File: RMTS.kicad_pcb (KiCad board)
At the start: 2 copper layers, 80 x 50.2 mm, 54 parts, among them J1 USB_B, J10 CONN_02, J2 Programmer, J3 Screw_Terminal_01x03, J4 Screw_Terminal_01x04, J5 Screw_Terminal_01x02, J6 Screw_Terminal_01x02, J7 Micro_SD_Card_Det_Hirose_DM3AT, J8 CONN_03, J9 CONN_02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

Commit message: Fixed mistakes
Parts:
- C11, C12: value C -> 0.1uF
- DRDY: value TestPoint -> DRDY
- R10, R9: value R_US -> 1k
- SCL: value TestPoint -> SCL
- SDA: value TestPoint -> SDA
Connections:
- U3 pad 8: /VBUS -> GND
- U3 pad 9: GND -> /VBUS
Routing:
- net /VBUS: track 128.1 -> 126.5 mm, vias 2 -> 1
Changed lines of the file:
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@@
     (thickness 1.6)
     (drawings 22)
-    (tracks 467)
+    (tracks 468)
     (zones 0)
     (modules 54)
@@
       (effects (font (size 1 1) (thickness 0.15)))
     )
-    (fp_text value TestPoint (at 0 1.55) (layer F.Fab)
+    (fp_text value SCL (at 0 1.55) (layer F.Fab)
       (effects (font (size 1 1) (thickness 0.15)))
     )
@@
       (effects (font (size 1 1) (thickness 0.15)))
     )
-    (fp_text value TestPoint (at 0 1.55) (layer F.Fab)
+    (fp_text value SDA (at 0 1.55) (layer F.Fab)
       (effects (font (size 1 1) (thickness 0.15)))
     )
@@
       (effects (font (size 1 1) (thickness 0.15)))
     )
-    (fp_text value TestPoint (at 0 1.55) (layer F.Fab)
+    (fp_text value DRDY (at 0 1.55) (layer F.Fab)
       (effects (font (size 1 1) (thickness 0.15)))
     )
@@
       (effects (font (size 1 1) (thickness 0.15)))
     )
-    (fp_text value C (at 0 1.65) (layer F.Fab)
+    (fp_text value 0.1uF (at 0 1.65) (layer F.Fab)
       (effects (font (size 1 1) (thickness 0.15)))
     )
@@
       (effects (font (size 1 1) (thickness 0.15)))
     )
-    (fp_text value C (at 0 1.65) (layer F.Fab)
+    (fp_text value 0.1uF (at 0 1.65) (layer F.Fab)
       (effects (font (size 1 1) (thickness 0.15)))
     )
@@
       (effects (font (size 1 1) (thickness 0.15)))
     )
-    (fp_text value R_US (at 0 1.65) (layer F.Fab)
+    (fp_text value 1k (at 0 1.65) (layer F.Fab)
       (effects (font (size 1 1) (thickness 0.15)))
     )
@@
       (effects (font (size 1 1) (thickness 0.15)))
     )
-    (fp_text value R_US (at 0 1.65) (layer F.Fab)
+    (fp_text value 1k (at 0 1.65) (layer F.Fab)
       (effects (font (size 1 1) (thickness 0.15)))
     )
@@
       (net 18 "Net-(J3-Pad3)"))
     (pad 8 smd rect (at -2.95 2.275 90) (size 1.5 0.45) (layers F.Cu F.Paste F.Mask)
+      (net 1 GND))
+    (pad 9 smd rect (at 2.95 2.275 90) (size 1.5 0.45) (layers F.Cu F.Paste F.Mask)
       (net 2 /VBUS))
-    (pad 9 smd rect (at 2.95 2.275 90) (size 1.5 0.45) (layers F.Cu F.Paste F.Mask)
-      (net 1 GND))
     (pad 10 smd rect (at 2.95 1.625 90) (size 1.5 0.45) (layers F.Cu F.Paste F.Mask)
       (net 1 GND))
@@
   (segment (start 201.54 104.53) (end 201.295 104.775) (width 0.2) (layer F.Cu) (net 1))
   (segment (start 201.54 102.87) (end 201.54 104.53) (width 0.2) (layer F.Cu) (net 1))
-  (via (at 202.184 93.726) (size 0.6) (drill 0.4) (layers F.Cu B.Cu) (net 1))
   (via (at 181.61 93.98) (size 0.6) (drill 0.4) (layers F.Cu B.Cu) (net 1))
   (segment (start 181.61 93.98) (end 181.61 95.25) (width 0.2) (layer F.Cu) (net 1))
@@
   (via (at 144.272 106.68) (size 0.6) (drill 0.4) (layers F.Cu B.Cu) (net 1))
   (segment (start 145.415 93.345) (end 145.415 94.615) (width 0.5) (layer F.Cu) (net 1))
-  (segment (start 201.665 94.245) (end 202.184 93.726) (width 0.2) (layer F.Cu) (net 1))
-  (segment (start 201.665 94.84) (end 201.665 94.245) (width 0.2) (layer F.Cu) (net 1))
-  (segment (start 201.759736 93.726) (end 202.184 93.726) (width 0.2) (layer F.Cu) (net 1))
-  (segment (start 201.179 93.726) (end 201.759736 93.726) (width 0.2) (layer F.Cu) (net 1))
-  (segment (start 201.015 93.89) (end 201.179 93.726) (width 0.2) (layer F.Cu) (net 1))
-  (segment (start 201.015 94.84) (end 201.015 93.89) (width 0.2) (layer F.Cu) (net 1))
   (segment (start 146.831 70.212) (end 147.066 69.977) (width 0.2) (layer F.Cu) (net 2))
   (via (at 199.39 96.52) (size 0.6) (drill 0.4) (layers F.Cu B.Cu) (net 2))
-  (via (at 201.93 99.06) (size 0.6) (drill 0.4) (layers F.Cu B.Cu) (net 2))
-  (segment (start 201.93 100.475) (end 201.665 100.74) (width 0.2) (layer F.Cu) (net 2))
-  (segment (start 201.93 99.06) (end 201.93 100.475) (width 0.2) (layer F.Cu) (net 2))
   (segment (start 147.131271 92.667999) (end 151.638 97.174728) (width 0.5) (layer F.Cu) (net 2))
   (segment (start 142.24 90.805) (end 144.102999 92.667999) (width 0.5) (layer F.Cu) (net 2))
@@
   (segment (start 199.715 94.84) (end 199.715 95.79) (width 0.2) (layer F.Cu) (net 2))
   (segment (start 199.715 95.79) (end 199.39 96.115) (width 0.2) (layer F.Cu) (net 2))
-  (segment (start 199.39 101.6) (end 201.93 99.06) (width 0.2) (layer B.Cu) (net 2))
   (segment (start 199.39 96.52) (end 199.39 101.6) (width 0.2) (layer B.Cu) (net 2))
   (segment (start 199.39 101.6) (end 199.39 108.37418) (width 0.2) (layer B.Cu) (net 2))
@@
   (segment (start 141.764 80.8) (end 139.054 83.51) (width 1) (layer B.Cu) (net 1))
   (segment (start 141.764 78.74) (end 141.764 80.8) (width 1) (layer B.Cu) (net 1))
+  (segment (start 201.665 99.79) (end 201.665 100.74) (width 0.2) (layer F.Cu) (net 1))
+  (segment (start 201.665 99.640736) (end 201.665 99.79) (width 0.2) (layer F.Cu) (net 1))
+  (segment (start 201.084264 99.06) (end 201.665 99.640736) (width 0.2) (layer F.Cu) (net 1))
+  (segment (start 200.66 99.06) (end 201.084264 99.06) (width 0.2) (layer F.Cu) (net 1))
+  (segment (start 201.015 95.79) (end 200.666 96.139) (width 0.2) (layer F.Cu) (net 1))
+  (segment (start 201.015 94.84) (end 201.015 95.79) (width 0.2) (layer F.Cu) (net 1))
+  (segment (start 200.666 96.139) (end 200.533 96.139) (width 0.2) (layer F.Cu) (net 1))
+  (via (at 200.533 96.139) (size 0.6) (drill 0.4) (layers F.Cu B.Cu) (net 1))
   (segment (start 146.939 69.85) (end 147.066 69.977) (width 0.5) (layer F.Cu) (net 2))
   (segment (start 143.764 78.74) (end 142.536999 79.967001) (width 0.5) (layer F.Cu) (net 2))
@@
   (segment (start 141.175039 79.967001) (end 140.074961 78.866923) (width 0.5) (layer F.Cu) (net 2))
   (segment (start 143.764 78.74) (end 143.579962 78.74) (width 0.5) (layer F.Cu) (net 2))
+  (segment (start 201.665 95.79) (end 201.665 94.84) (width 0.2) (layer F.Cu) (net 2))
+  (segment (start 200.635001 96.819999) (end 201.665 95.79) (width 0.2) (layer F.Cu) (net 2))
+  (segment (start 199.39 96.52) (end 199.689999 96.819999) (width 0.2) (layer F.Cu) (net 2))
+  (segment (start 199.689999 96.819999) (end 200.635001 96.819999) (width 0.2) (layer F.Cu) (net 2))
   (segment (start 198.2275 96.6275) (end 199.065 95.79) (width 0.2) (layer F.Cu) (net 3))
   (segment (start 167.71348 78.575) (end 167.71348 79.375) (width 0.2) (layer F.Cu) (net 3))

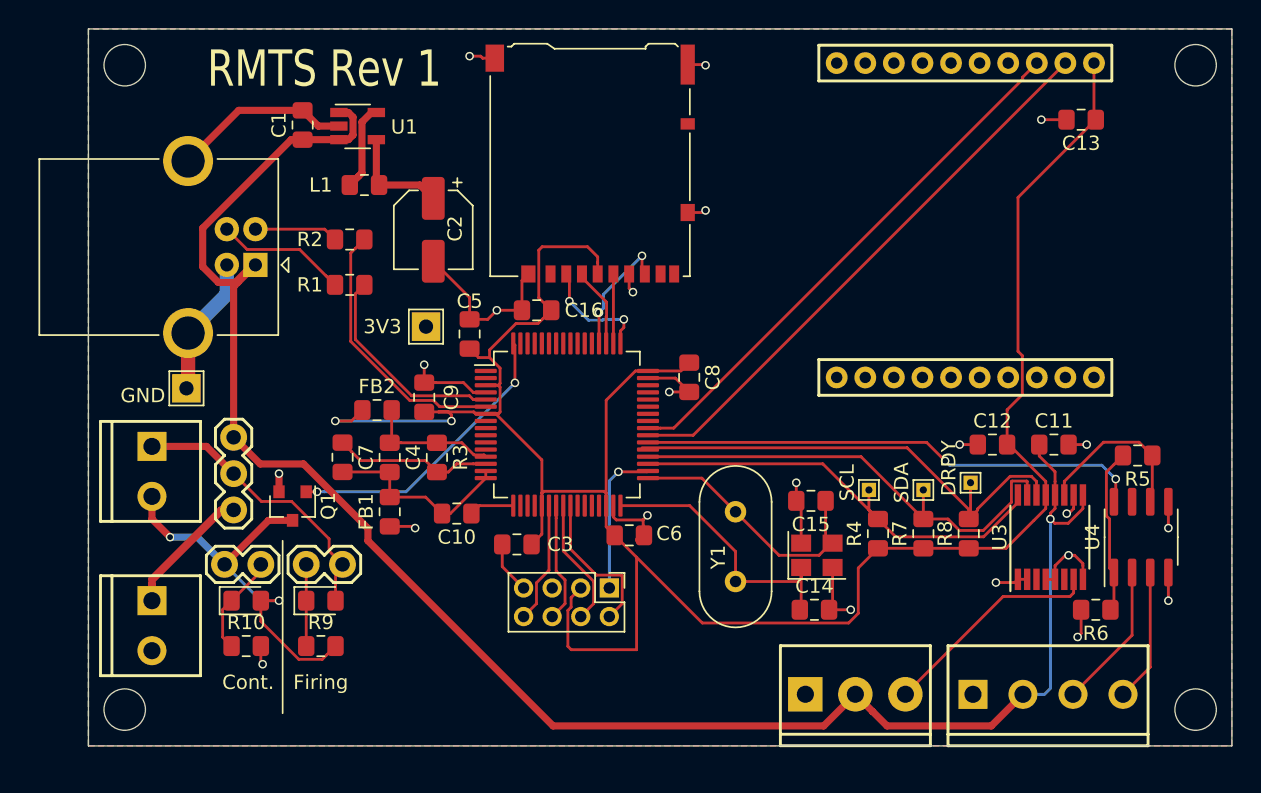
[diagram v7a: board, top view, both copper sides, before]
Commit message: Pulled ADC enable high, added diode to firing circuit, rerouted some traces
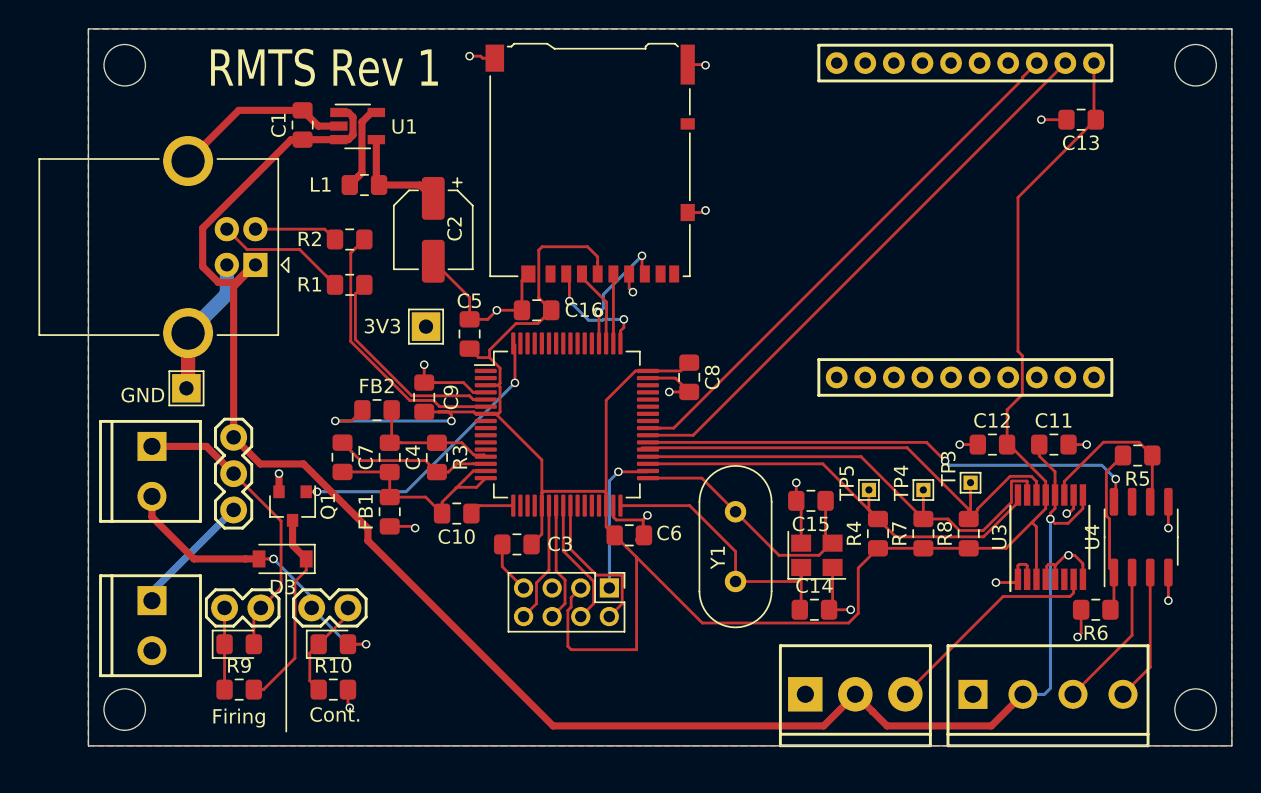
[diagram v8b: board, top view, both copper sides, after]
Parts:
- added D3: D, Diode_SMD:D_SOD-123, F.Cu at (145.7, 99.3)
- moved D2 6.82 mm to (149.2, 105.3)
- moved J10 6.82 mm to (147.7, 102.7)
- moved R10 6.82 mm to (149.2, 108.5)
- moved D1 6.48 mm to (142.6, 105.3)
- moved J9 6.48 mm to (141.6, 102.7)
- moved R9 6.48 mm to (142.6, 108.5)
- renumbered DRDY to TP3, SDA to TP4, SCL to TP5
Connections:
- Q1 pad 3: Net-(D2-Pad2) -> Net-(D3-Pad1)
- R9 pad 2: Net-(D2-Pad2) -> Net-(D3-Pad1)
- U3 pad 3: /ARESET -> +3V3
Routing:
- net Net-(D3-Pad1): track 0.00 -> 14.3 mm
- net Net-(J5-Pad1): track 18.3 -> 9.93 mm
- net Net-(D2-Pad2): track 28.3 -> 22.0 mm
- net +3V3: track 169.5 -> 173.6 mm
- net GND: track 91.4 -> 94.3 mm
- net Net-(C10-Pad2): track 13.8 -> 16.4 mm
- net Net-(D1-Pad2): track 20.0 -> 20.6 mm
